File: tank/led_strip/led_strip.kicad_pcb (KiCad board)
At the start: 2 copper layers, 54 x 10.8 mm, 9 parts, among them J1 Conn_01x04_Male

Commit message: LED strip version 0.2
- fix orientation of LED footprints
- fix unconnected traces (DOH.)
- attempt to use local footprint library
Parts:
- moved D1 2.50 mm to (108.8, 97.8), turned to 180 degrees
- moved D2 2.50 mm to (135.2, 97.8), turned to 180 degrees
- moved D3 2.50 mm to (122.0, 97.8), turned to 180 degrees
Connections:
- D2 pad 1: Net-(D2-Pad1) -> Net-(D1-Pad1)
- D2 pad 2: Net-(D1-Pad2) -> Net-(D2-Pad2)
- D3 pad 1: Net-(D3-Pad1) -> Net-(D1-Pad1)
- D3 pad 2: Net-(D1-Pad2) -> Net-(D3-Pad2)
- J1 pad 1: Net-(D1-Pad2) -> Net-(D1-Pad1)
- R1 pad 1: Net-(D1-Pad1) -> Net-(D1-Pad2)
- R2 pad 1: Net-(D2-Pad1) -> Net-(D2-Pad2)
- R3 pad 1: Net-(D3-Pad1) -> Net-(D3-Pad2)
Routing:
- net Net-(D1-Pad1): track 10.1 -> 54.2 mm
- net Net-(D1-Pad2): track 52.5 -> 10.1 mm
- net Net-(D2-Pad2): track 0.00 -> 14.8 mm
- net Net-(D2-Pad1): track 14.8 -> 0.00 mm
- net Net-(D3-Pad2): track 0.00 -> 10.1 mm
- net Net-(D3-Pad1): track 10.1 -> 0.00 mm
- net Net-(J1-Pad2): track 17.2 -> 18.9 mm
- net Net-(J1-Pad4): track 30.9 -> 32.6 mm
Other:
- board text added: "LED Strip Version 0.2"
- board text added: "MIAR Labs - nick.groesz@gmail.com"

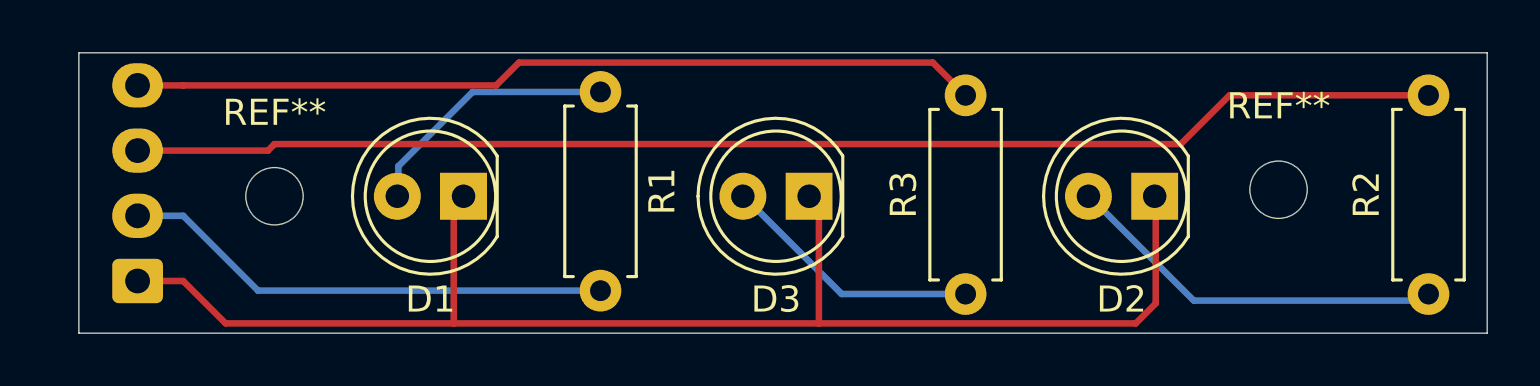
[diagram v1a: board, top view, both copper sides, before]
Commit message: LED version 0.3 - Cannot believe I screwed-up the footprints twice in a row. - Made a little wider for mounting-hole
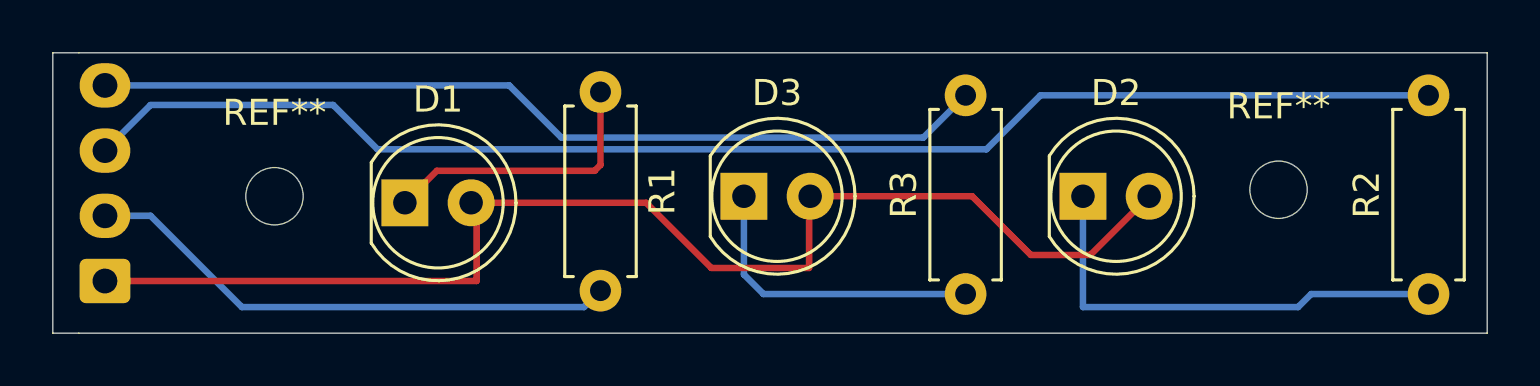
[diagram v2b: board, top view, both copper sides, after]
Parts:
- moved D2 2.75 mm to (132.5, 97.8), turned to 0 degrees
- moved D3 2.50 mm to (119.5, 97.8), turned to 0 degrees
- moved D1 2.26 mm to (106.5, 98.0), turned to 0 degrees
- moved J1 1.25 mm to (95.0, 101.0)
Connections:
- D2 pad 1: Net-(D1-Pad1) -> Net-(D2-Pad1)
- D2 pad 2: Net-(D2-Pad2) -> Net-(D1-Pad2)
- D3 pad 1: Net-(D1-Pad1) -> Net-(D3-Pad1)
- D3 pad 2: Net-(D3-Pad2) -> Net-(D1-Pad2)
- J1 pad 1: Net-(D1-Pad1) -> Net-(D1-Pad2)
- R1 pad 1: Net-(D1-Pad2) -> Net-(D1-Pad1)
- R2 pad 1: Net-(D2-Pad2) -> Net-(D2-Pad1)
- R3 pad 1: Net-(D3-Pad2) -> Net-(D3-Pad1)
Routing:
- net Net-(D1-Pad1): track 54.2 -> 10.9 mm
- net Net-(D1-Pad2): track 10.1 -> 49.0 mm
- net Net-(D2-Pad1): track 0.00 -> 17.7 mm
- net Net-(D2-Pad2): track 14.8 -> 0.00 mm
- net Net-(D3-Pad1): track 0.00 -> 11.8 mm
- net Net-(D3-Pad2): track 10.1 -> 0.00 mm
- net Net-(J1-Pad3): track 50.4 -> 53.0 mm
- net Net-(J1-Pad4): track 32.6 -> 34.5 mm
- net Net-(J1-Pad2): track 18.9 -> 20.7 mm
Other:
- board size 54 x 10.8 mm -> 55 x 10.8 mm
- board text added: "LED Strip Version 0.3"
- board text removed: "LED Strip Version 0.2"

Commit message: and all that jazz
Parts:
- moved D2 5.75 mm to (126.8, 97.9)
- moved R3 4.76 mm to (123.2, 101.8)
- moved R2 4.50 mm to (141.2, 101.5)
- moved REF** 4.26 mm to (135.8, 97.8)
- moved D3 2.26 mm to (117.2, 98.0)
- moved D1 1.21 mm to (107.7, 98.0)
- moved R1 0.45 mm to (113.8, 94.1)
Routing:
- net Net-(D1-Pad2): track 49.0 -> 37.5 mm
- net Net-(J1-Pad3): track 53.0 -> 47.1 mm
- net Net-(J1-Pad4): track 34.5 -> 28.9 mm
- net Net-(D3-Pad1): track 11.8 -> 7.55 mm
- net Net-(D1-Pad1): track 10.9 -> 7.64 mm
- net Net-(D2-Pad1): track 17.7 -> 16.0 mm
- net Net-(J1-Pad2): track 20.7 -> 20.1 mm
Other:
- board size 55 x 10.8 mm -> 50.5 x 10.8 mm
- board text added: "LED Strip Version 0.4"
- board text removed: "LED Strip Version 0.3"
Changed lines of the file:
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@@
     (thickness 1.6)
     (drawings 8)
-    (tracks 37)
+    (tracks 22)
     (zones 0)
     (modules 9)
@@
     (mod_text_size 1 1)
     (mod_text_width 0.15)
-    (pad_size 1.524 1.524)
-    (pad_drill 0.762)
+    (pad_size 3 3)
+    (pad_drill 3)
     (pad_to_mask_clearance 0.05)
     (aux_axis_origin 0 0)
@@
       (effects (font (size 1 1) (thickness 0.15)))
     )
-    (pad 1 np_thru_hole circle (at 0 0) (size 2.2 2.2) (drill 2.2) (layers *.Cu *.Mask))
+    (pad "" np_thru_hole circle (at 0 0) (size 3 3) (drill 3) (layers *.Cu *.Mask))
   )
   (module MountingHole:MountingHole_2.2mm_M2 (layer F.Cu)
-    (at 140 97.5)
+    (at 135.75 97.75)
     (descr "Mounting Hole 2.2mm, no annular, M2")
     (tags "mounting hole 2.2mm no annular m2")
@@
       (effects (font (size 1 1) (thickness 0.15)))
     )
-    (pad 1 np_thru_hole circle (at 0 0) (size 2.2 2.2) (drill 2.2) (layers *.Cu *.Mask))
+    (pad "" np_thru_hole circle (at 0 0) (size 3 3) (drill 3) (layers *.Cu *.Mask))
   )
   (module LED_THT:LED_D5.0mm (layer F.Cu)
-    (at 106.5 98)
+    (at 107.71 98)
     (descr "LED, diameter 5.0mm, 2 pins, http://cdn-reichelt.de/documents/datenblatt/A500/LL-504BC2E-009.pdf")
     (tags "LED diameter 5.0mm 2 pins")
@@
   )
   (module LED_THT:LED_D5.0mm (layer F.Cu)
-    (at 132.5 97.75)
+    (at 126.75 97.9)
     (descr "LED, diameter 5.0mm, 2 pins, http://cdn-reichelt.de/documents/datenblatt/A500/LL-504BC2E-009.pdf")
     (tags "LED diameter 5.0mm 2 pins")
@@
   )
   (module LED_THT:LED_D5.0mm (layer F.Cu)
-    (at 119.5 97.75)
+    (at 117.25 98)
     (descr "LED, diameter 5.0mm, 2 pins, http://cdn-reichelt.de/documents/datenblatt/A500/LL-504BC2E-009.pdf")
     (tags "LED diameter 5.0mm 2 pins")
@@
   )
   (module Resistor_THT:R_Axial_DIN0207_L6.3mm_D2.5mm_P7.62mm_Horizontal (layer F.Cu)
-    (at 114 93.75 270)
+    (at 113.75 94.13 270)
     (descr "Resistor, Axial_DIN0207 series, Axial, Horizontal, pin pitch=7.62mm, 0.25W = 1/4W, length*diameter=6.3*2.5mm^2, http://cdn-reichelt.de/documents/datenblatt/B400/1_4W%23YAG.pdf")
     (tags "Resistor Axial_DIN0207 series Axial Horizontal pin pitch 7.62mm 0.25W = 1/4W length 6.3mm diameter 2.5mm")
-    (fp_text reference R1 (at 3.81 -2.37 90) (layer F.SilkS)
+    (fp_text reference R1 (at 4.67 -2.3 90) (layer F.SilkS)
       (effects (font (size 1 1) (thickness 0.15)))
     )
@@
   )
   (module Resistor_THT:R_Axial_DIN0207_L6.3mm_D2.5mm_P7.62mm_Horizontal (layer F.Cu)
-    (at 145.75 101.5 90)
+    (at 141.25 101.5 90)
     (descr "Resistor, Axial_DIN0207 series, Axial, Horizontal, pin pitch=7.62mm, 0.25W = 1/4W, length*diameter=6.3*2.5mm^2, http://cdn-reichelt.de/documents/datenblatt/B400/1_4W%23YAG.pdf")
     (tags "Resistor Axial_DIN0207 series Axial Horizontal pin pitch 7.62mm 0.25W = 1/4W length 6.3mm diameter 2.5mm")
@@
   )
   (module Resistor_THT:R_Axial_DIN0207_L6.3mm_D2.5mm_P7.62mm_Horizontal (layer F.Cu)
-    (at 128 101.5 90)
+    (at 123.25 101.75 90)
     (descr "Resistor, Axial_DIN0207 series, Axial, Horizontal, pin pitch=7.62mm, 0.25W = 1/4W, length*diameter=6.3*2.5mm^2, http://cdn-reichelt.de/documents/datenblatt/B400/1_4W%23YAG.pdf")
     (tags "Resistor Axial_DIN0207 series Axial Horizontal pin pitch 7.62mm 0.25W = 1/4W length 6.3mm diameter 2.5mm")
@@
     (effects (font (size 1 1) (thickness 0.15)) (justify mirror))
   )
-  (gr_text "LED Strip Version 0.3" (at 120.75 99.5) (layer B.SilkS)
+  (gr_text "LED Strip Version 0.4" (at 120.75 99.5) (layer B.SilkS)
     (effects (font (size 1 1) (thickness 0.15)) (justify mirror))
   )
   (gr_line (start 93 103) (end 93 92.25) (layer Edge.Cuts) (width 0.05))
-  (gr_line (start 148 103) (end 94 103) (layer Edge.Cuts) (width 0.05))
-  (gr_line (start 148 92.25) (end 148 103) (layer Edge.Cuts) (width 0.05))
-  (gr_line (start 94 92.25) (end 148 92.25) (layer Edge.Cuts) (width 0.05))
-  (segment (start 107.725001 96.774999) (end 113.774999 96.774999) (width 0.25) (layer F.Cu) (net 1))
-  (segment (start 106.5 98) (end 107.725001 96.774999) (width 0.25) (layer F.Cu) (net 1))
-  (segment (start 114 96.549998) (end 114 93.75) (width 0.25) (layer F.Cu) (net 1))
-  (segment (start 113.774999 96.774999) (end 114 96.549998) (width 0.25) (layer F.Cu) (net 1))
-  (segment (start 95 101) (end 109.25 101) (width 0.25) (layer F.Cu) (net 2))
-  (segment (start 109.25 98.21) (end 109.04 98) (width 0.25) (layer F.Cu) (net 2))
-  (segment (start 109.25 101) (end 109.25 98.21) (width 0.25) (layer F.Cu) (net 2))
-  (segment (start 109.04 98) (end 115.75 98) (width 0.25) (layer F.Cu) (net 2))
-  (segment (start 115.75 98) (end 118.25 100.5) (width 0.25) (layer F.Cu) (net 2))
-  (segment (start 118.25 100.5) (end 122 100.5) (width 0.25) (layer F.Cu) (net 2))
-  (segment (start 122 97.79) (end 122.04 97.75) (width 0.25) (layer F.Cu) (net 2))
-  (segment (start 122 100.5) (end 122 97.79) (width 0.25) (layer F.Cu) (net 2))
-  (segment (start 122.04 97.75) (end 128.25 97.75) (width 0.25) (layer F.Cu) (net 2))
-  (segment (start 128.25 97.75) (end 130.5 100) (width 0.25) (layer F.Cu) (net 2))
-  (segment (start 132.79 100) (end 135.04 97.75) (width 0.25) (layer F.Cu) (net 2))
-  (segment (start 130.5 100) (end 132.79 100) (width 0.25) (layer F.Cu) (net 2))
-  (segment (start 95 98.5) (end 96.75 98.5) (width 0.25) (layer B.Cu) (net 3))
-  (segment (start 96.75 98.5) (end 100.25 102) (width 0.25) (layer B.Cu) (net 3))
-  (segment (start 113.37 102) (end 114 101.37) (width 0.25) (layer B.Cu) (net 3))
-  (segment (start 100.25 102) (end 113.37 102) (width 0.25) (layer B.Cu) (net 3))
-  (segment (start 103.75 94.25) (end 96.75 94.25) (width 0.25) (layer B.Cu) (net 4))
-  (segment (start 105.45001 95.95001) (end 103.75 94.25) (width 0.25) (layer B.Cu) (net 4))
-  (segment (start 128.79999 95.95001) (end 105.45001 95.95001) (width 0.25) (layer B.Cu) (net 4))
-  (segment (start 96.75 94.25) (end 95 96) (width 0.25) (layer B.Cu) (net 4))
-  (segment (start 130.87 93.88) (end 128.79999 95.95001) (width 0.25) (layer B.Cu) (net 4))
-  (segment (start 145.75 93.88) (end 130.87 93.88) (width 0.25) (layer B.Cu) (net 4))
-  (segment (start 95 93.5) (end 110.5 93.5) (width 0.25) (layer B.Cu) (net 5))
-  (segment (start 110.5 93.5) (end 112.5 95.5) (width 0.25) (layer B.Cu) (net 5))
-  (segment (start 126.38 95.5) (end 128 93.88) (width 0.25) (layer B.Cu) (net 5))
-  (segment (start 112.5 95.5) (end 126.38 95.5) (width 0.25) (layer B.Cu) (net 5))
-  (segment (start 132.5 97.75) (end 132.5 102) (width 0.25) (layer B.Cu) (net 6))
-  (segment (start 141.25 101.5) (end 145.75 101.5) (width 0.25) (layer B.Cu) (net 6))
-  (segment (start 140.75 102) (end 141.25 101.5) (width 0.25) (layer B.Cu) (net 6))
-  (segment (start 132.5 102) (end 140.75 102) (width 0.25) (layer B.Cu) (net 6))
-  (segment (start 119.5 97.75) (end 119.5 100.75) (width 0.25) (layer B.Cu) (net 7))
-  (segment (start 120.25 101.5) (end 128 101.5) (width 0.25) (layer B.Cu) (net 7))
-  (segment (start 119.5 100.75) (end 120.25 101.5) (width 0.25) (layer B.Cu) (net 7))
+  (gr_line (start 143.5 103) (end 94 103) (layer Edge.Cuts) (width 0.05))
+  (gr_line (start 143.5 92.25) (end 143.5 103) (layer Edge.Cuts) (width 0.05))
+  (gr_line (start 94 92.25) (end 143.5 92.25) (layer Edge.Cuts) (width 0.05))
+  (segment (start 111.58 94.13) (end 113.75 94.13) (width 0.25) (layer F.Cu) (net 1))
+  (segment (start 107.71 98) (end 111.58 94.13) (width 0.25) (layer F.Cu) (net 1))
+  (segment (start 107.25 101) (end 110.25 98) (width 0.25) (layer F.Cu) (net 2))
+  (segment (start 95 101) (end 107.25 101) (width 0.25) (layer F.Cu) (net 2))
+  (segment (start 118.564999 99.225001) (end 119.79 98) (width 0.25) (layer F.Cu) (net 2))
+  (segment (start 111.475001 99.225001) (end 118.564999 99.225001) (width 0.25) (layer F.Cu) (net 2))
+  (segment (start 110.25 98) (end 111.475001 99.225001) (width 0.25) (layer F.Cu) (net 2))
+  (segment (start 128.064999 99.125001) (end 129.29 97.9) (width 0.25) (layer F.Cu) (net 2))
+  (segment (start 120.915001 99.125001) (end 128.064999 99.125001) (width 0.25) (layer F.Cu) (net 2))
+  (segment (start 119.79 98) (end 120.915001 99.125001) (width 0.25) (layer F.Cu) (net 2))
+  (segment (start 98.25 101.75) (end 113.75 101.75) (width 0.25) (layer B.Cu) (net 3))
+  (segment (start 95 98.5) (end 98.25 101.75) (width 0.25) (layer B.Cu) (net 3))
+  (segment (start 139.205001 95.924999) (end 141.25 93.88) (width 0.25) (layer B.Cu) (net 4))
+  (segment (start 95.075001 95.924999) (end 139.205001 95.924999) (width 0.25) (layer B.Cu) (net 4))
+  (segment (start 95 96) (end 95.075001 95.924999) (width 0.25) (layer B.Cu) (net 4))
+  (segment (start 122.124999 93.004999) (end 123.25 94.13) (width 0.25) (layer B.Cu) (net 5))
+  (segment (start 95.495001 93.004999) (end 122.124999 93.004999) (width 0.25) (layer B.Cu) (net 5))
+  (segment (start 95 93.5) (end 95.495001 93.004999) (width 0.25) (layer B.Cu) (net 5))
+  (segment (start 130.35 101.5) (end 141.25 101.5) (width 0.25) (layer B.Cu) (net 6))
+  (segment (start 126.75 97.9) (end 130.35 101.5) (width 0.25) (layer B.Cu) (net 6))
+  (segment (start 121 101.75) (end 123.25 101.75) (width 0.25) (layer B.Cu) (net 7))
+  (segment (start 117.25 98) (end 121 101.75) (width 0.25) (layer B.Cu) (net 7))
 )

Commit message: Major cleanup. I localized all the footprint and symbol libraries.
I deleted most of the rescue stuff.

I still need to finish-up changes to the turret board.

Now this checkout should work "out of the box".
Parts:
- D1, D2, D3: footprint LED_THT:LED_D5.0mm -> custom:LED_D5.0mm
- J1: footprint Connector_JST:JST_EH_B4B-EH-A_1x04_P2.50mm_Vertical -> custom:JST_EH_B4B-EH-A_1x04_P2.50mm_Vertical
- R1, R2, R3: footprint Resistor_THT:R_Axial_DIN0207_L6.3mm_D2.5mm_P7.62mm_Horizontal -> custom:R_Axial_DIN0207_L6.3mm_D2.5mm_P7.62mm_Horizontal
- moved J1 0.64 mm to (94.6, 101.5)
